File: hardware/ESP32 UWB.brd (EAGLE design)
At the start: 72.3 x 32.6 mm, 56 parts, among them J2 HEADER-12P-2.54, J3 10118194-0001LF, Q1 S8050, Q2 S8050, SW1 BUTTON, SW2 BUTTON, U1 AMS1117-3.3, U2 ESP32-C3-MINI-1-N4, U3 SILICON_LABS_CP2102N-A01-GQFN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, U4 DWM1000

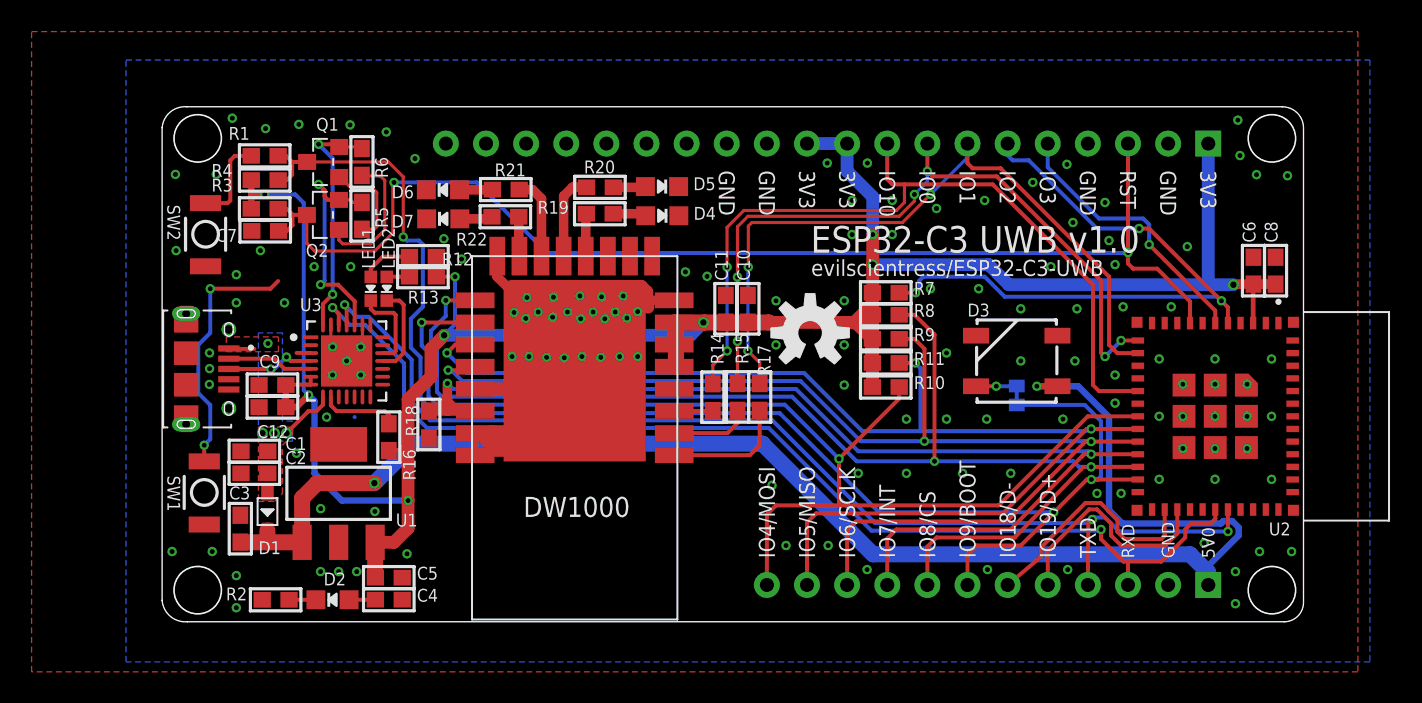
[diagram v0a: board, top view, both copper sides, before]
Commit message: replaced WS2812 with SK6812-mini-e
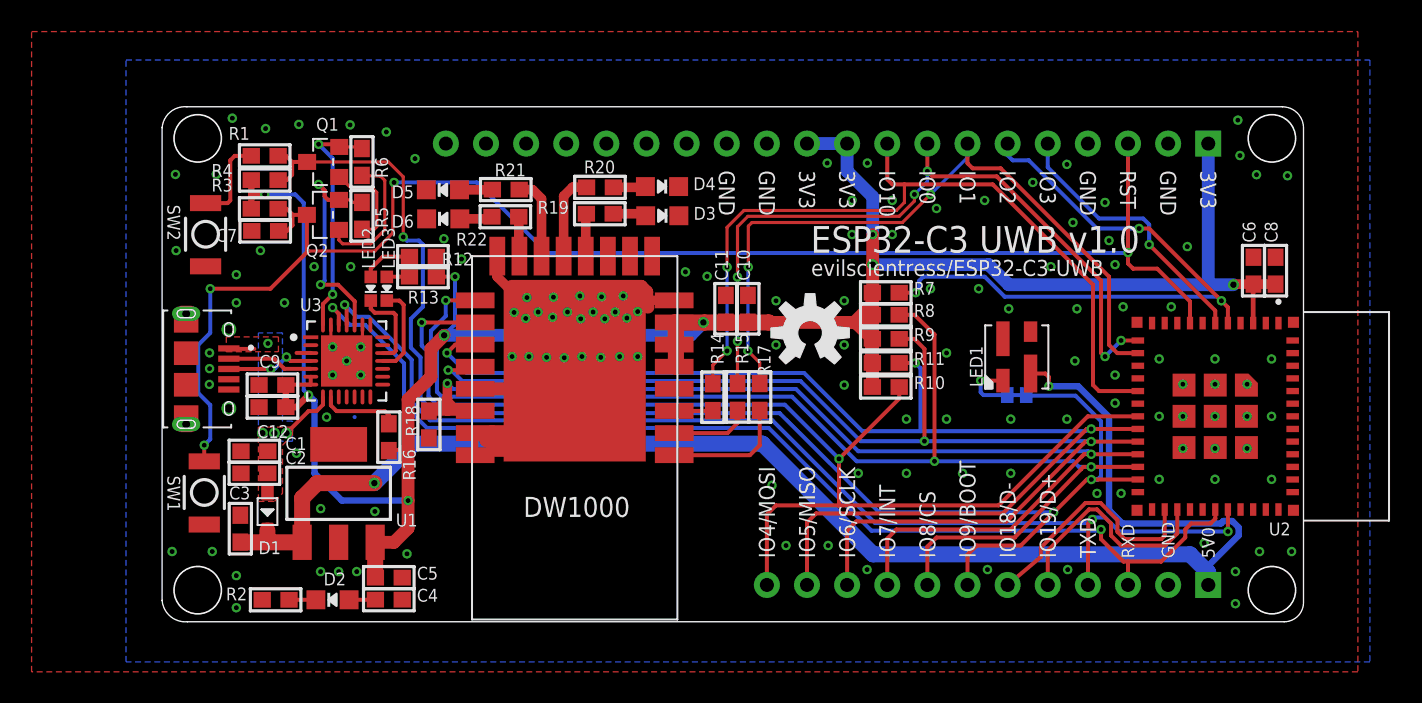
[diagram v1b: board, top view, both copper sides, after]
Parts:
- removed D7: GREEN, microbuilder:CHIPLED_0805_NOOUTLINE
- added LED3: RED, isystems:CHIPLED_0603_NOOUTLINE
- D3: value WS2812B -> GREEN; device SparkFun-LED:WS2812B -> microbuilder:CHIPLED_0805_NOOUTLINE
- LED1: value BLUE -> (none); device isystems:CHIPLED_0603_NOOUTLINE -> SK6812:LED3535
- LED2: value RED -> BLUE
- moved LED1 41.1 mm to (53.8, 16.8), turned to 90 degrees
- moved D3 24.2 mm to (31.4, 25.7), turned to 270 degrees
- moved D5 13.9 mm to (17.5, 27.3), turned to 90 degrees
- moved D4 1.85 mm to (31.4, 27.5)
- moved D6 1.84 mm to (17.5, 25.5)
- moved LED2 1.02 mm to (13.0, 21.1)
- turned SJ1 to 0 degrees
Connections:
- net GND: now also D3.C, LED1.2-GND; no longer D3.3, D7.C
- net IO9: now also LED1.3-DIN; no longer D3.4
- net N$1: now also D3.A; no longer D4.A
- net N$16: now also D4.A; no longer D5.A
- net N$17: now also D5.A; no longer D6.A
- net N$18: now also D6.A; no longer D7.A
- net N$2: now also LED2.A; no longer LED1.A
- net N$3: now also LED2.C; no longer LED1.C
- net N$4: now also LED3.A; no longer LED2.A
- net N$6: now also LED3.C; no longer LED2.C
- net VDD5V: now also LED1.4-VDD; no longer D3.1
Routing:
- net RESET: track 93.5 -> 96.5 mm
- net IO9: track 97.6 -> 98.6 mm
- net GND: vias 137 -> 136
